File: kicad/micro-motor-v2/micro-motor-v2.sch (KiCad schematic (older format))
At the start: 5 parts

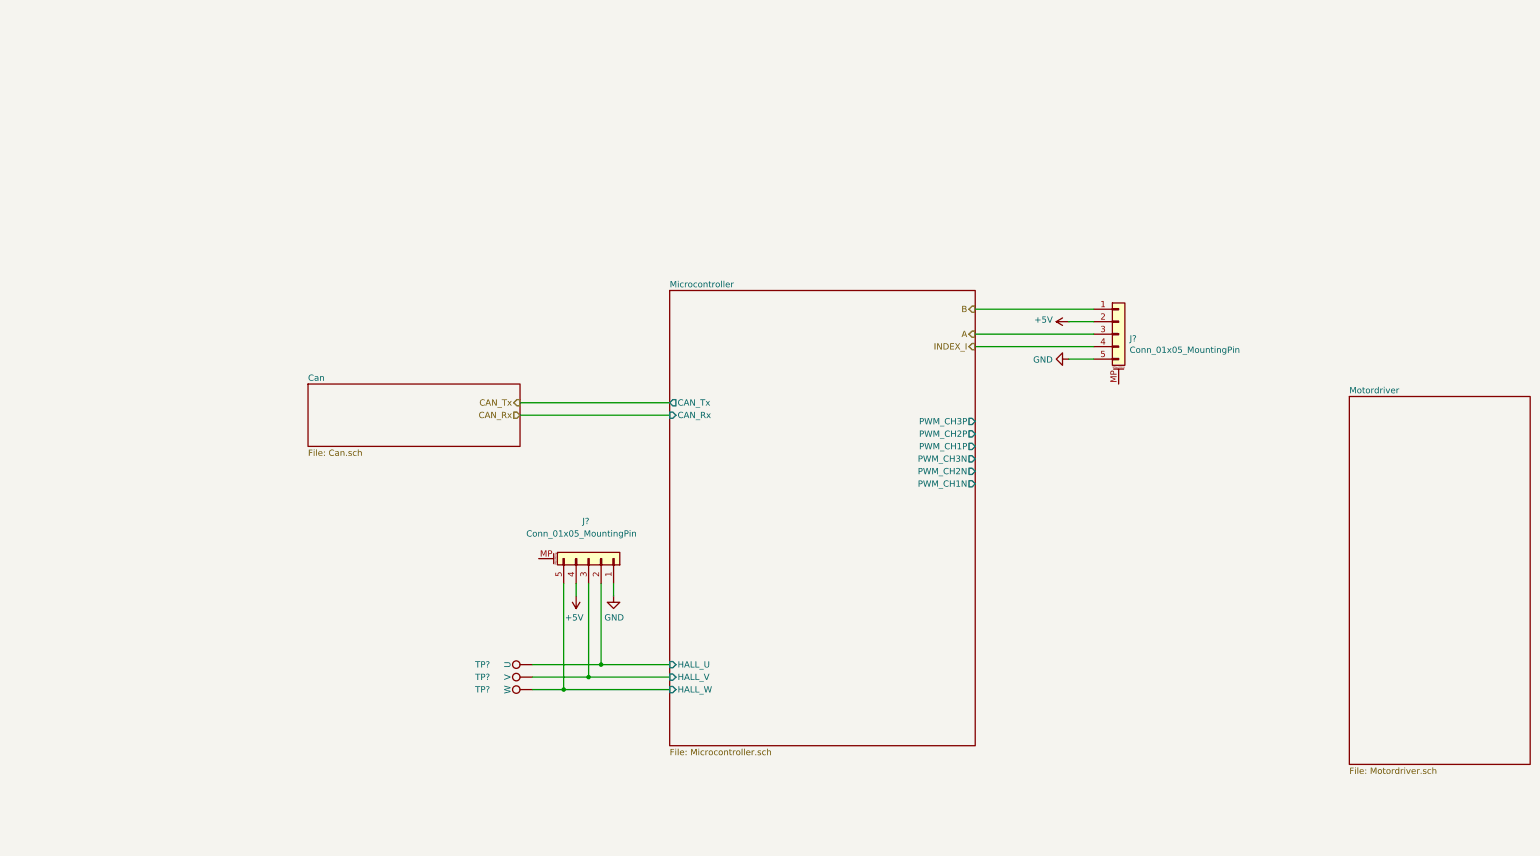
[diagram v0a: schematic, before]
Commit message: micro-motor-v2: Schematic continued
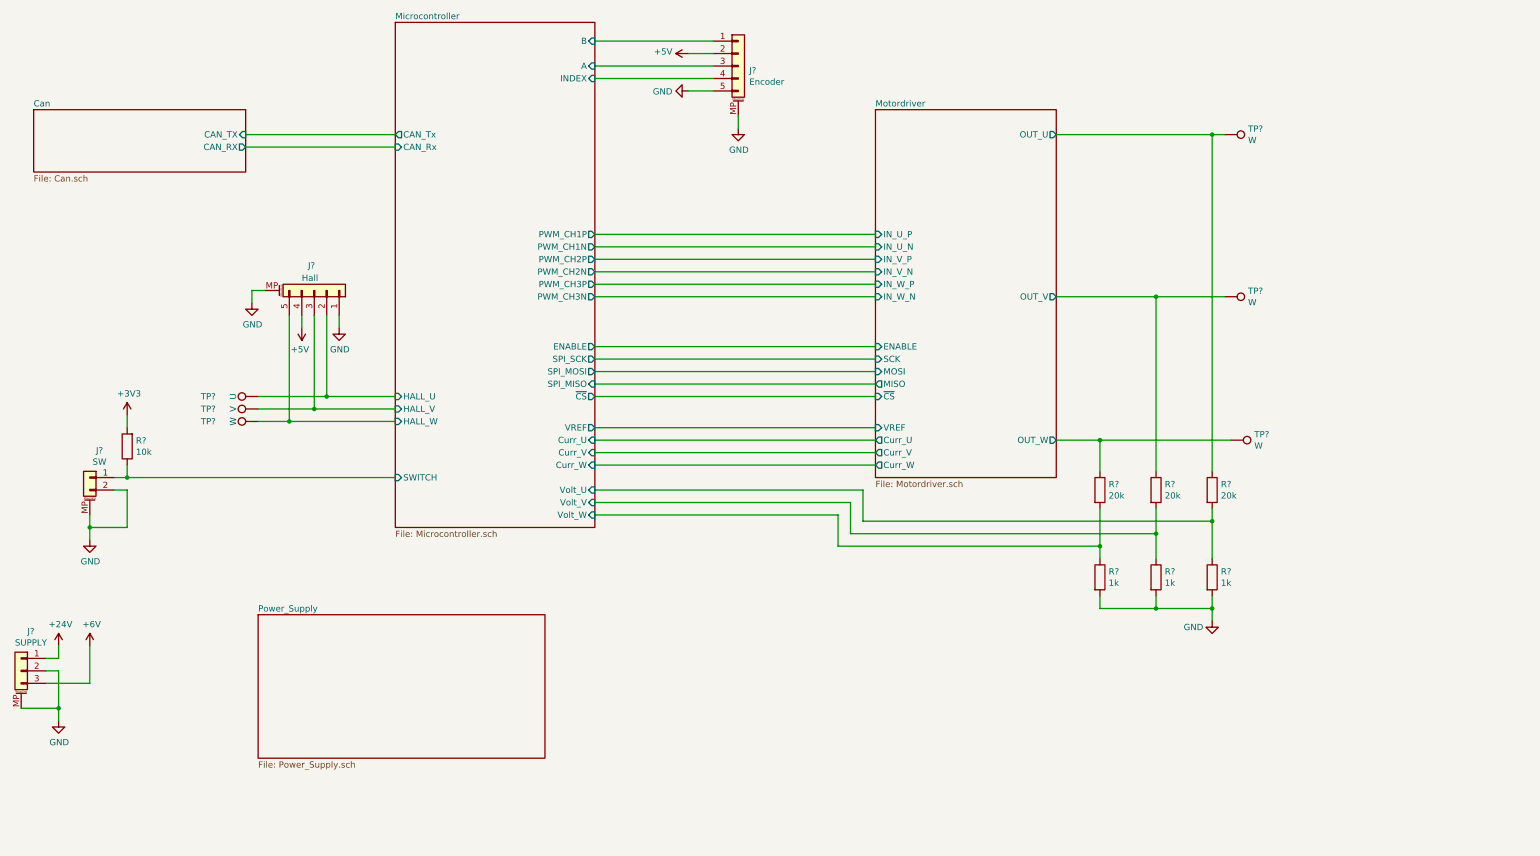
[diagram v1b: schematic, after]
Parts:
- added J?: SW, symbol Connector_Generic_MountingPin:Conn_01x02_MountingPin
- added J?: SUPPLY, symbol Connector_Generic_MountingPin:Conn_01x03_MountingPin
- added R? (x3): 20k, symbol Device:R
- added R? (x3): 1k, symbol Device:R
- added R?: 10k, symbol Device:R
- added TP? (x3): W, symbol Connector:TestPoint
- J?: value Conn_01x05_MountingPin -> Hall
- J?: value Conn_01x05_MountingPin -> Encoder
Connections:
- net GND: now also J?.MP (MountPin), J?.MP (MountPin), J?.2 (Pin_2), J?.2 (Pin_2), J?.MP (MountPin), J?.MP (MountPin), R?.2, R?.2, R?.2
- net A renamed Microcontroller/A
- net B renamed Microcontroller/B
- net INDEX_I renamed Microcontroller/INDEX
- new net +24V: J?.1 (Pin_1)
- new net +3V3: R?.2
- new net +6V: J?.3 (Pin_3)
- new net Microcontroller/SWITCH: J?.1 (Pin_1), R?.1
- new net Microcontroller/Volt_U: R?.1, R?.2
- new net Microcontroller/Volt_V: R?.1, R?.2
- new net Microcontroller/Volt_W: R?.1, R?.2
- new net Motordriver/OUT_U: R?.1, TP?.1
- new net Motordriver/OUT_V: R?.1, TP?.1
- new net Motordriver/OUT_W: R?.1, TP?.1
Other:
- moved on the sheet: J?, TP?

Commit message: micro-motor-v2: Schematic finished
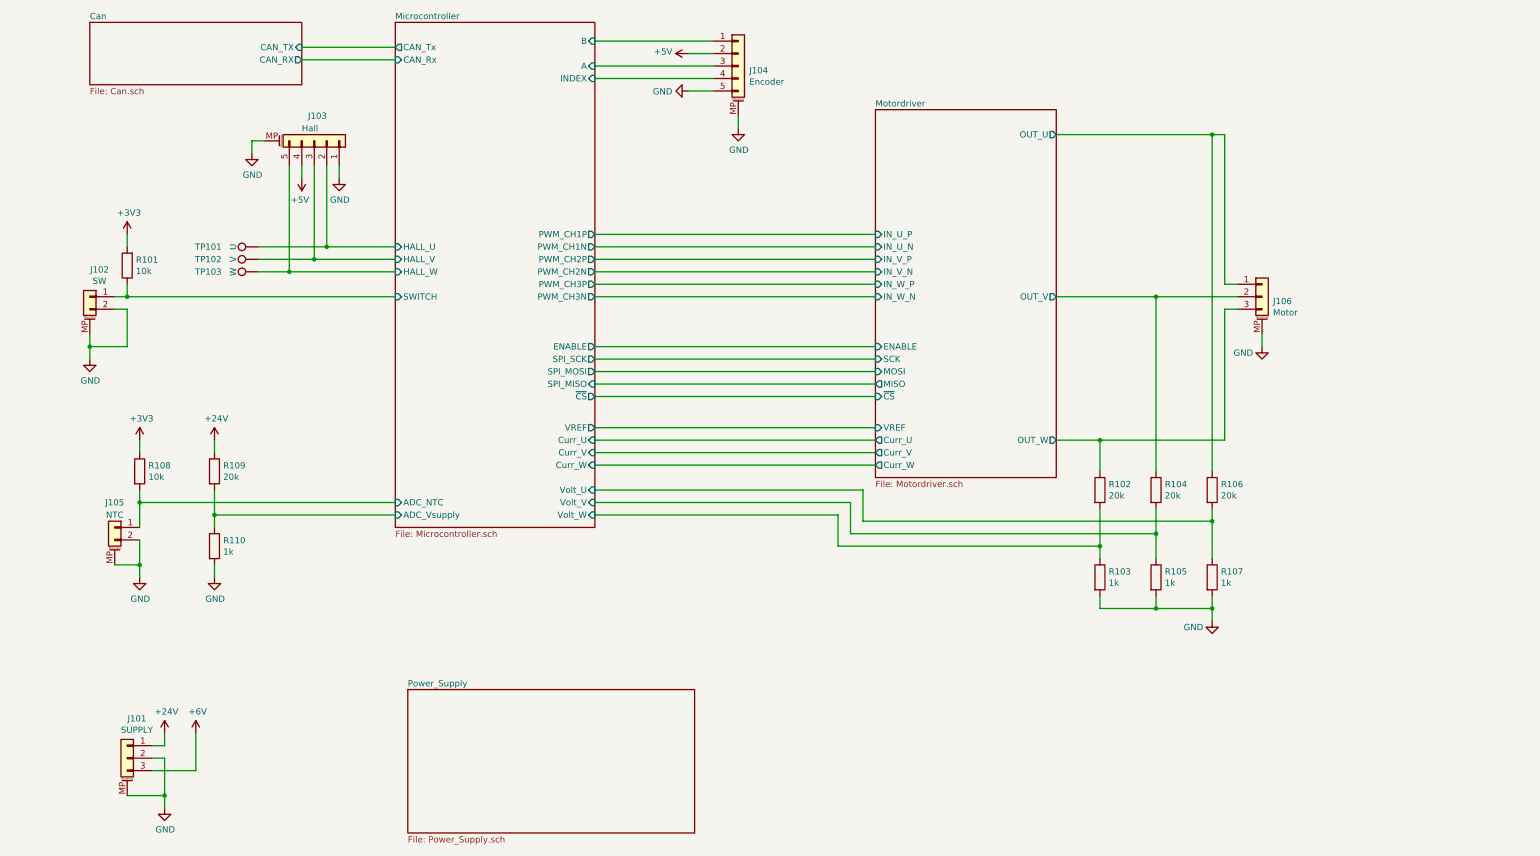
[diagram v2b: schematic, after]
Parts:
- removed TP? (x3): W, symbol Connector:TestPoint
- added J105: NTC, Connector_JST:JST_GH_BM02B-GHS-TBT_1x02-1MP_P1.25mm_Vertical, symbol Connector_Generic_MountingPin:Conn_01x02_MountingPin
- added J106: Motor, Connector_JST:JST_XH_B3B-XH-A_1x03_P2.50mm_Vertical, symbol Connector_Generic_MountingPin:Conn_01x03_MountingPin
- added R108: 10k, Resistor_SMD:R_0402_1005Metric, symbol Device:R
- added R109: 20k, Resistor_SMD:R_0402_1005Metric, symbol Device:R
- added R110: 1k, Resistor_SMD:R_0402_1005Metric, symbol Device:R
- J101: renamed from J?; footprint (none) -> Connector_JST:JST_XH_B3B-XH-A_1x03_P2.50mm_Vertical
- J102: renamed from J?; footprint (none) -> Connector_JST:JST_GH_BM02B-GHS-TBT_1x02-1MP_P1.25mm_Vertical
- J103, J104: renamed from J?; footprint (none) -> Connector_JST:JST_GH_BM05B-GHS-TBT_1x05-1MP_P1.25mm_Vertical
- R101, R102, R103, R104, R105, R106, R107: renamed from R?; footprint (none) -> Resistor_SMD:R_0402_1005Metric
- TP101, TP102, TP103: renamed from TP?; footprint (none) -> TestPoint:TestPoint_Pad_D1.0mm
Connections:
- net +24V: now also R109.1
- net +3V3: now also R108.1
- net GND: now also J105.2 (Pin_2), J105.MP (MountPin), J106.MP (MountPin), R110.2
- net Motordriver/OUT_U: now also J106.1 (Pin_1)
- net Motordriver/OUT_V: now also J106.2 (Pin_2)
- net Motordriver/OUT_W: now also J106.3 (Pin_3)
- new net Microcontroller/ADC_NTC: J105.1 (Pin_1), R108.2
- new net Microcontroller/ADC_Vsupply: R109.2, R110.1
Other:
- moved on the sheet: J101, J102, J103, R101, TP101, TP102, TP103

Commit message: micro-motor-v2: layout: components placed
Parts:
- added R111, R112, R113: 10k, Resistor_SMD:R_0402_1005Metric, symbol Device:R
- J101, J106: symbol Connector_Generic_MountingPin:Conn_01x03_MountingPin -> Connector_Generic:Conn_01x03
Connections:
- net +5V: now also R111.1, R112.1, R113.1
- net GND: no longer J101.MP (MountPin), J106.MP (MountPin)
- net Microcontroller/HALL_U: now also R113.2
- net Microcontroller/HALL_V: now also R112.2
- net Microcontroller/HALL_W: now also R111.2
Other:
- moved on the sheet: J103
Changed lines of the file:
@@
 L Connector_Generic_MountingPin:Conn_01x05_MountingPin J103
 U 1 1 5DCC1C32
-P 3150 1850
-F 0 "J103" V 3350 1800 50  0000 L CNN
-F 1 "Hall" V 3250 1750 50  0000 L CNN
-F 2 "Connector_JST:JST_GH_BM05B-GHS-TBT_1x05-1MP_P1.25mm_Vertical" H 3150 1850 50  0001 C CNN
-F 3 "~" H 3150 1850 50  0001 C CNN
-	1    3150 1850
-	0    1    -1   0
-$EndComp
-Wire Wire Line
-	2950 2050 2950 2900
+P 3150 3850
+F 0 "J103" V 3350 3800 50  0000 L CNN
+F 1 "Hall" V 3250 3750 50  0000 L CNN
+F 2 "Connector_JST:JST_GH_BM05B-GHS-TBT_1x05-1MP_P1.25mm_Vertical" H 3150 3850 50  0001 C CNN
+F 3 "~" H 3150 3850 50  0001 C CNN
+	1    3150 3850
+	0    1    1    0
+$EndComp
 Connection ~ 2950 2900
 Wire Wire Line
 	2950 2900 3800 2900
-Wire Wire Line
-	3150 2050 3150 2800
 Connection ~ 3150 2800
 Wire Wire Line
@@
 Wire Wire Line
 	2700 2700 3250 2700
-Wire Wire Line
-	3250 2050 3250 2700
 Connection ~ 3250 2700
 Wire Wire Line
@@
 L power:GND #PWR0108
 U 1 1 5DCD04C9
-P 3350 2150
-F 0 "#PWR0108" H 3350 1900 50  0001 C CNN
-F 1 "GND" H 3355 1977 50  0000 C CNN
-F 2 "" H 3350 2150 50  0001 C CNN
-F 3 "" H 3350 2150 50  0001 C CNN
-	1    3350 2150
+P 3450 3650
+F 0 "#PWR0108" H 3450 3400 50  0001 C CNN
+F 1 "GND" H 3455 3477 50  0000 C CNN
+F 2 "" H 3450 3650 50  0001 C CNN
+F 3 "" H 3450 3650 50  0001 C CNN
+	1    3450 3650
 	1    0    0    -1
 $EndComp
@@
 L power:+5V #PWR0107
 U 1 1 5DCD0A88
-P 3050 2150
-F 0 "#PWR0107" H 3050 2000 50  0001 C CNN
-F 1 "+5V" H 3065 2323 50  0000 C CNN
-F 2 "" H 3050 2150 50  0001 C CNN
-F 3 "" H 3050 2150 50  0001 C CNN
-	1    3050 2150
-	-1   0    0    1
-$EndComp
-Wire Wire Line
-	3050 2050 3050 2150
-Wire Wire Line
-	3350 2050 3350 2150
+P 3050 3550
+F 0 "#PWR0107" H 3050 3400 50  0001 C CNN
+F 1 "+5V" H 3065 3723 50  0000 C CNN
+F 2 "" H 3050 3550 50  0001 C CNN
+F 3 "" H 3050 3550 50  0001 C CNN
+	1    3050 3550
+	1    0    0    -1
+$EndComp
+Wire Wire Line
+	3050 3650 3050 3550
+Wire Wire Line
+	3450 3550 3450 3650
 $Sheet
 S 3800 900  1600 4050
@@
 F3 "HALL_V" I L 3800 2800 50
 F4 "HALL_W" I L 3800 2900 50
-F5 "CAN_Tx" O L 3800 1100 50
-F6 "CAN_Rx" I L 3800 1200 50
-F7 "PWM_CH3P" O R 5400 3000 50
-F8 "PWM_CH2P" O R 5400 2800 50
-F9 "PWM_CH1P" O R 5400 2600 50
-F10 "PWM_CH3N" O R 5400 3100 50
-F11 "PWM_CH2N" O R 5400 2900 50
-F12 "PWM_CH1N" O R 5400 2700 50
-F13 "A" I R 5400 1250 50
-F14 "B" I R 5400 1050 50
-F15 "INDEX" I R 5400 1350 50
-F16 "Curr_U" I R 5400 4250 50
-F17 "Curr_V" I R 5400 4350 50
-F18 "Curr_W" I R 5400 4450 50
-F19 "Volt_U" I R 5400 4650 50
-F20 "Volt_V" I R 5400 4750 50
-F21 "Volt_W" I R 5400 4850 50
-F22 "SPI_MOSI" O R 5400 3700 50
-F23 "SPI_MISO" I R 5400 3800 50
-F24 "SPI_SCK" O R 5400 3600 50
-F25 "SWITCH" I L 3800 3100 50
-F26 "~CS" O R 5400 3900 50
-F27 "ENABLE" O R 5400 3500 50
-F28 "VREF" O R 5400 4150 50
-F29 "ADC_NTC" I L 3800 4750 50
-F30 "ADC_Vsupply" I L 3800 4850 50
+F5 "PWM_CH3P" O R 5400 3000 50
+F6 "PWM_CH2P" O R 5400 2800 50
+F7 "PWM_CH1P" O R 5400 2600 50
+F8 "PWM_CH3N" O R 5400 3100 50
+F9 "PWM_CH2N" O R 5400 2900 50
+F10 "PWM_CH1N" O R 5400 2700 50
+F11 "A" I R 5400 1250 50
+F12 "B" I R 5400 1050 50
+F13 "INDEX" I R 5400 1350 50
+F14 "Curr_U" I R 5400 4250 50
+F15 "Curr_V" I R 5400 4350 50
+F16 "Curr_W" I R 5400 4450 50
+F17 "Volt_U" I R 5400 4650 50
+F18 "Volt_V" I R 5400 4750 50
+F19 "Volt_W" I R 5400 4850 50
+F20 "SPI_MOSI" O R 5400 3700 50
+F21 "SPI_MISO" I R 5400 3800 50
+F22 "SPI_SCK" O R 5400 3600 50
+F23 "SWITCH" I L 3800 3100 50
+F24 "~CS" O R 5400 3900 50
+F25 "ENABLE" O R 5400 3500 50
+F26 "VREF" O R 5400 4150 50
+F27 "ADC_NTC" I L 3800 4750 50
+F28 "ADC_Vsupply" I L 3800 4850 50
+F29 "CAN_TX" O L 3800 1100 50
+F30 "CAN_RX" I L 3800 1200 50
 $EndSheet
 $Comp
@@
 $EndSheet
 $Comp
-L Connector_Generic_MountingPin:Conn_01x03_MountingPin J101
-U 1 1 5DDFB168
-P 1650 6800
-F 0 "J101" H 1572 7117 50  0000 C CNN
-F 1 "SUPPLY" H 1572 7026 50  0000 C CNN
-F 2 "Connector_JST:JST_XH_B3B-XH-A_1x03_P2.50mm_Vertical" H 1650 6800 50  0001 C CNN
-F 3 "~" H 1650 6800 50  0001 C CNN
-	1    1650 6800
-	-1   0    0    -1
-$EndComp
-$Comp
 L power:+24V #PWR0101
 U 1 1 5DDFBBDE
@@
 $EndComp
 Wire Wire Line
-	1950 7200 1950 7100
-Wire Wire Line
 	1950 6800 1850 6800
-Wire Wire Line
-	1650 7100 1950 7100
-Connection ~ 1950 7100
-Wire Wire Line
-	1950 7100 1950 6800
 $Comp
 L power:GND #PWR0106
 U 1 1 5DE09726
-P 2650 1950
-F 0 "#PWR0106" H 2650 1700 50  0001 C CNN
-F 1 "GND" H 2655 1777 50  0000 C CNN
-F 2 "" H 2650 1950 50  0001 C CNN
-F 3 "" H 2650 1950 50  0001 C CNN
-	1    2650 1950
-	1    0    0    -1
-$EndComp
-Wire Wire Line
-	2650 1950 2650 1850
-Wire Wire Line
-	2650 1850 2750 1850
+P 2650 3950
+F 0 "#PWR0106" H 2650 3700 50  0001 C CNN
+F 1 "GND" H 2655 3777 50  0000 C CNN
+F 2 "" H 2650 3950 50  0001 C CNN
+F 3 "" H 2650 3950 50  0001 C CNN
+	1    2650 3950
+	1    0    0    -1
+$EndComp
+Wire Wire Line
+	2650 3950 2650 3850
+Wire Wire Line
+	2650 3850 2750 3850
 $Comp
 L power:GND #PWR0111
@@
 Connection ~ 1750 5250
 $Comp
-L Connector_Generic_MountingPin:Conn_01x03_MountingPin J106
+L Connector_Generic:Conn_01x03 J106
 U 1 1 5D9E796C
 P 10750 3100
@@
 	10450 4250 9450 4250
 $Comp
-L power:GND #PWR0118
-U 1 1 5D9F39A2
-P 10750 3500
-F 0 "#PWR0118" H 10750 3250 50  0001 C CNN
-F 1 "GND" H 10600 3450 50  0000 C CNN
-F 2 "" H 10750 3500 50  0001 C CNN
-F 3 "" H 10750 3500 50  0001 C CNN
-	1    10750 3500
-	1    0    0    -1
-$EndComp
-Wire Wire Line
-	10750 3500 10750 3400
+L Connector_Generic:Conn_01x03 J101
+U 1 1 5DDFB168
+P 1650 6800
+F 0 "J101" H 1572 7117 50  0000 C CNN
+F 1 "SUPPLY" H 1572 7026 50  0000 C CNN
+F 2 "Connector_JST:JST_XH_B3B-XH-A_1x03_P2.50mm_Vertical" H 1650 6800 50  0001 C CNN
+F 3 "~" H 1650 6800 50  0001 C CNN
+	1    1650 6800
+	-1   0    0    -1
+$EndComp
+Wire Wire Line
+	1950 6800 1950 7200
+Wire Wire Line
+	3350 3650 3350 3550
+Wire Wire Line
+	3350 3550 3450 3550
+Wire Wire Line
+	3250 2700 3250 3650
+Wire Wire Line
+	3150 3650 3150 2800
+Wire Wire Line
+	2950 2900 2950 3650
+$Comp
+L Device:R R?
+U 1 1 5DC6332F
+P 2950 2350
+AR Path="/5D99156F/5DC6332F" Ref="R?"  Part="1"
+AR Path="/5DC6332F" Ref="R111"  Part="1"
+F 0 "R111" H 3020 2396 50  0000 L CNN
+F 1 "10k" H 3020 2305 50  0000 L CNN
+F 2 "Resistor_SMD:R_0402_1005Metric" V 2880 2350 50  0001 C CNN
+F 3 "~" H 2950 2350 50  0001 C CNN
+	1    2950 2350
+	1    0    0    -1
+$EndComp
+$Comp
+L Device:R R?
+U 1 1 5DC636E4
+P 3150 2350
+AR Path="/5D99156F/5DC636E4" Ref="R?"  Part="1"
+AR Path="/5DC636E4" Ref="R112"  Part="1"
+F 0 "R112" H 3220 2396 50  0000 L CNN
+F 1 "10k" H 3220 2305 50  0000 L CNN
+F 2 "Resistor_SMD:R_0402_1005Metric" V 3080 2350 50  0001 C CNN
+F 3 "~" H 3150 2350 50  0001 C CNN
+	1    3150 2350
+	1    0    0    -1
+$EndComp
+$Comp
+L Device:R R?
+U 1 1 5DC6398A
+P 3250 2350
+AR Path="/5D99156F/5DC6398A" Ref="R?"  Part="1"
+AR Path="/5DC6398A" Ref="R113"  Part="1"
+F 0 "R113" H 3320 2396 50  0000 L CNN
+F 1 "10k" H 3320 2305 50  0000 L CNN
+F 2 "Resistor_SMD:R_0402_1005Metric" V 3180 2350 50  0001 C CNN
+F 3 "~" H 3250 2350 50  0001 C CNN
+	1    3250 2350
+	1    0    0    -1
+$EndComp
+Wire Wire Line
+	2950 2500 2950 2900
+Wire Wire Line
+	3150 2800 3150 2500
+Wire Wire Line
+	3250 2500 3250 2700
+$Comp
+L power:+5V #PWR0119
+U 1 1 5DC6D040
+P 3050 2000
+F 0 "#PWR0119" H 3050 1850 50  0001 C CNN
+F 1 "+5V" H 3065 2173 50  0000 C CNN
+F 2 "" H 3050 2000 50  0001 C CNN
+F 3 "" H 3050 2000 50  0001 C CNN
+	1    3050 2000
+	1    0    0    -1
+$EndComp
+Wire Wire Line
+	3050 2000 3050 2100
+Wire Wire Line
+	3050 2100 2950 2100
+Wire Wire Line
+	2950 2100 2950 2200
+Wire Wire Line
+	3050 2100 3150 2100
+Wire Wire Line
+	3250 2100 3250 2200
+Connection ~ 3050 2100
+Wire Wire Line
+	3150 2200 3150 2100
+Connection ~ 3150 2100
+Wire Wire Line
+	3150 2100 3250 2100
 $EndSCHEMATC

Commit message: micro-motor-v2: Layout...
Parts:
- added R114: 0, Resistor_SMD:R_0402_1005Metric, symbol Device:R
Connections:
- net GND: now also R114.1; no longer J101.2 (Pin_2)
- new net GNDPWR: J101.2 (Pin_2), R114.2
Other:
- moved on the sheet: J101
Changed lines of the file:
@@
 L power:+24V #PWR0101
 U 1 1 5DDFBBDE
-P 1950 6600
-F 0 "#PWR0101" H 1950 6450 50  0001 C CNN
-F 1 "+24V" H 1965 6773 50  0000 C CNN
-F 2 "" H 1950 6600 50  0001 C CNN
-F 3 "" H 1950 6600 50  0001 C CNN
-	1    1950 6600
-	1    0    0    -1
-$EndComp
-Wire Wire Line
-	1950 6600 1950 6700
-Wire Wire Line
-	1950 6700 1850 6700
-Wire Wire Line
-	1850 6900 2200 6900
-Wire Wire Line
-	2200 6900 2200 6600
+P 1700 6500
+F 0 "#PWR0101" H 1700 6350 50  0001 C CNN
+F 1 "+24V" H 1715 6673 50  0000 C CNN
+F 2 "" H 1700 6500 50  0001 C CNN
+F 3 "" H 1700 6500 50  0001 C CNN
+	1    1700 6500
+	1    0    0    -1
+$EndComp
+Wire Wire Line
+	1700 6500 1700 6600
+Wire Wire Line
+	1700 6600 1600 6600
+Wire Wire Line
+	1600 6800 1950 6800
+Wire Wire Line
+	1950 6800 1950 6500
 $Comp
 L power:+6V #PWR0104
 U 1 1 5DDFFA47
-P 2200 6600
-F 0 "#PWR0104" H 2200 6450 50  0001 C CNN
-F 1 "+6V" H 2215 6773 50  0000 C CNN
-F 2 "" H 2200 6600 50  0001 C CNN
-F 3 "" H 2200 6600 50  0001 C CNN
-	1    2200 6600
-	1    0    0    -1
-$EndComp
-$Comp
-L power:GND #PWR0102
-U 1 1 5DDFFED2
-P 1950 7200
-F 0 "#PWR0102" H 1950 6950 50  0001 C CNN
-F 1 "GND" H 1955 7027 50  0000 C CNN
-F 2 "" H 1950 7200 50  0001 C CNN
-F 3 "" H 1950 7200 50  0001 C CNN
-	1    1950 7200
-	1    0    0    -1
-$EndComp
-Wire Wire Line
-	1950 6800 1850 6800
+P 1950 6500
+F 0 "#PWR0104" H 1950 6350 50  0001 C CNN
+F 1 "+6V" H 1965 6673 50  0000 C CNN
+F 2 "" H 1950 6500 50  0001 C CNN
+F 3 "" H 1950 6500 50  0001 C CNN
+	1    1950 6500
+	1    0    0    -1
+$EndComp
+Wire Wire Line
+	1700 6700 1600 6700
 $Comp
 L power:GND #PWR0106
@@
 L Connector_Generic:Conn_01x03 J101
 U 1 1 5DDFB168
-P 1650 6800
-F 0 "J101" H 1572 7117 50  0000 C CNN
-F 1 "SUPPLY" H 1572 7026 50  0000 C CNN
-F 2 "Connector_JST:JST_XH_B3B-XH-A_1x03_P2.50mm_Vertical" H 1650 6800 50  0001 C CNN
-F 3 "~" H 1650 6800 50  0001 C CNN
-	1    1650 6800
+P 1400 6700
+F 0 "J101" H 1322 7017 50  0000 C CNN
+F 1 "SUPPLY" H 1322 6926 50  0000 C CNN
+F 2 "Connector_JST:JST_XH_B3B-XH-A_1x03_P2.50mm_Vertical" H 1400 6700 50  0001 C CNN
+F 3 "~" H 1400 6700 50  0001 C CNN
+	1    1400 6700
 	-1   0    0    -1
 $EndComp
 Wire Wire Line
-	1950 6800 1950 7200
+	1700 6700 1700 7000
 Wire Wire Line
 	3350 3650 3350 3550
@@
 Wire Wire Line
 	3150 2100 3250 2100
+$Comp
+L power:GNDPWR #PWR0102
+U 1 1 5D959FF4
+P 1700 7100
+F 0 "#PWR0102" H 1700 6900 50  0001 C CNN
+F 1 "GNDPWR" H 1704 6946 50  0000 C CNN
+F 2 "" H 1700 7050 50  0001 C CNN
+F 3 "" H 1700 7050 50  0001 C CNN
+	1    1700 7100
+	1    0    0    -1
+$EndComp
+$Comp
+L Device:R R114
+U 1 1 5D95A486
+P 2150 7000
+F 0 "R114" V 1943 7000 50  0000 C CNN
+F 1 "0" V 2034 7000 50  0000 C CNN
+F 2 "Resistor_SMD:R_0402_1005Metric" V 2080 7000 50  0001 C CNN
+F 3 "~" H 2150 7000 50  0001 C CNN
+	1    2150 7000
+	0    1    1    0
+$EndComp
+$Comp
+L power:GND #PWR0120
+U 1 1 5D95ACB9
+P 2500 7100
+F 0 "#PWR0120" H 2500 6850 50  0001 C CNN
+F 1 "GND" H 2505 6927 50  0000 C CNN
+F 2 "" H 2500 7100 50  0001 C CNN
+F 3 "" H 2500 7100 50  0001 C CNN
+	1    2500 7100
+	1    0    0    -1
+$EndComp
+Wire Wire Line
+	2000 7000 1700 7000
+Connection ~ 1700 7000
+Wire Wire Line
+	1700 7000 1700 7100
+Wire Wire Line
+	2300 7000 2500 7000
+Wire Wire Line
+	2500 7000 2500 7100
 $EndSCHEMATC
